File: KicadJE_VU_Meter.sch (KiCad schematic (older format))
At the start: 62 parts, among them J1 Out, J2 In1, J3 In2, P1 HEADER_2x5_Doepfer, U1 TL072, U2 TL072

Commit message: Update KicadJE_VU_Meter.sch
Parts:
- added H6: Jack, AJ:Jack_6m3, symbol Mechanical:MountingHole_Pad
- added H7, H8, H?: Jack, AJ:Jack_3m5, symbol Mechanical:MountingHole_Pad
- added J?: Out, Connector_PinHeader_2.54mm:PinHeader_1x03_P2.54mm_Vertical_SMD_Pin1Right, symbol Connector:Conn_01x03_Male
- added MES2: VU Meter Backlight, Connector_PinHeader_2.54mm:PinHeader_1x02_P2.54mm_Vertical_SMD_Pin1Right, symbol Device:Amperemeter_AC
- added R?: 1k, Resistor_SMD:R_0805_2012Metric_Pad1.20x1.40mm_HandSolder, symbol Device:R
- added R?: OPEN, Resistor_SMD:R_0805_2012Metric_Pad1.20x1.40mm_HandSolder, symbol Device:R
- added TP?: Out, TestPoint:TestPoint_Pad_D2.0mm, symbol Connector:TestPoint
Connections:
- net -12VA: now also MES2.1
- net GND: now also H6.1, H7.1, H8.1, H?.1, MES2.2
- net Out1: now also R?.1
- new net: J?.2 (Pin_2), R?.2, R?.2
- new net: J?.1 (Pin_1), R?.1, TP?.1
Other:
- moved on the sheet: H5
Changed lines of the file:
@@
 L Mechanical:MountingHole H5
 U 1 1 5EF9702E
-P 9100 4750
-F 0 "H5" H 9200 4796 50  0000 L CNN
-F 1 "Meter" H 9200 4705 50  0000 L CNN
-F 2 "AJ:VU_Meter_Hole" H 9100 4750 50  0001 C CNN
-F 3 "~" H 9100 4750 50  0001 C CNN
-	1    9100 4750
+P 8850 4675
+F 0 "H5" H 8950 4721 50  0000 L CNN
+F 1 "Meter" H 8950 4630 50  0000 L CNN
+F 2 "AJ:VU_Meter_Hole" H 8850 4675 50  0001 C CNN
+F 3 "~" H 8850 4675 50  0001 C CNN
+	1    8850 4675
 	1    0    0    -1
 $EndComp
@@
 Wire Wire Line
 	1950 7100 1950 7475
+$Comp
+L Device:Amperemeter_AC MES2
+U 1 1 60A9F992
+P 9300 5150
+F 0 "MES2" H 9453 5196 50  0000 L CNN
+F 1 "VU Meter Backlight" H 9453 5105 50  0000 L CNN
+F 2 "Connector_PinHeader_2.54mm:PinHeader_1x02_P2.54mm_Vertical_SMD_Pin1Right" V 9300 5250 50  0001 C CNN
+F 3 "~" V 9300 5250 50  0001 C CNN
+	1    9300 5150
+	1    0    0    -1
+$EndComp
+$Comp
+L KicadJE_VU_Meter-rescue:GND-Envelope-cache-2018-08-04-13-00-04-KicadJE_Util-rescue #PWR0101
+U 1 1 60AA0119
+P 9150 4825
+AR Path="/60AA0119" Ref="#PWR0101"  Part="1"
+AR Path="/5C8C5FC0/60AA0119" Ref="#PWR?"  Part="1"
+AR Path="/5CAAE8D3/60AA0119" Ref="#PWR?"  Part="1"
+AR Path="/5E4B0DD9/60AA0119" Ref="#PWR?"  Part="1"
+AR Path="/5E62ACA1/60AA0119" Ref="#PWR?"  Part="1"
+AR Path="/5F49A670/60AA0119" Ref="#PWR?"  Part="1"
+F 0 "#PWR0101" H 9150 4575 50  0001 C CNN
+F 1 "GND" H 9155 4652 50  0000 C CNN
+F 2 "" H 9150 4825 50  0001 C CNN
+F 3 "" H 9150 4825 50  0001 C CNN
+	1    9150 4825
+	1    0    0    -1
+$EndComp
+$Comp
+L power:-12VA #PWR?
+U 1 1 60AA116C
+P 9300 5425
+AR Path="/5E4B0DD9/60AA116C" Ref="#PWR?"  Part="1"
+AR Path="/5E62ACA1/60AA116C" Ref="#PWR?"  Part="1"
+AR Path="/5F49A670/60AA116C" Ref="#PWR?"  Part="1"
+AR Path="/60AA116C" Ref="#PWR0102"  Part="1"
+F 0 "#PWR0102" H 9300 5275 50  0001 C CNN
+F 1 "-12VA" H 9450 5500 50  0000 C CNN
+F 2 "" H 9300 5425 50  0001 C CNN
+F 3 "" H 9300 5425 50  0001 C CNN
+	1    9300 5425
+	-1   0    0    1
+$EndComp
+Wire Wire Line
+	9300 5425 9300 5350
+Wire Wire Line
+	9300 4950 9300 4800
+Wire Wire Line
+	9300 4800 9150 4800
+Wire Wire Line
+	9150 4800 9150 4825
+$Comp
+L Mechanical:MountingHole_Pad H7
+U 1 1 60ABB9E2
+P 1500 2700
+F 0 "H7" H 1600 2749 50  0000 L CNN
+F 1 "Jack" H 1600 2658 50  0000 L CNN
+F 2 "AJ:Jack_3m5" H 1500 2700 50  0001 C CNN
+F 3 "~" H 1500 2700 50  0001 C CNN
+	1    1500 2700
+	1    0    0    -1
+$EndComp
+$Comp
+L Mechanical:MountingHole_Pad H8
+U 1 1 60ABC029
+P 1500 4075
+F 0 "H8" H 1600 4124 50  0000 L CNN
+F 1 "Jack" H 1600 4033 50  0000 L CNN
+F 2 "AJ:Jack_3m5" H 1500 4075 50  0001 C CNN
+F 3 "~" H 1500 4075 50  0001 C CNN
+	1    1500 4075
+	1    0    0    -1
+$EndComp
+$Comp
+L KicadJE_VU_Meter-rescue:GND-Envelope-cache-2018-08-04-13-00-04-KicadJE_Util-rescue #PWR0103
+U 1 1 60ABC354
+P 1500 4175
+AR Path="/60ABC354" Ref="#PWR0103"  Part="1"
+AR Path="/5C8C5FC0/60ABC354" Ref="#PWR?"  Part="1"
+AR Path="/5CAAE8D3/60ABC354" Ref="#PWR?"  Part="1"
+AR Path="/5E4B0DD9/60ABC354" Ref="#PWR?"  Part="1"
+AR Path="/5E62ACA1/60ABC354" Ref="#PWR?"  Part="1"
+AR Path="/5F49A670/60ABC354" Ref="#PWR?"  Part="1"
+F 0 "#PWR0103" H 1500 3925 50  0001 C CNN
+F 1 "GND" H 1505 4002 50  0000 C CNN
+F 2 "" H 1500 4175 50  0001 C CNN
+F 3 "" H 1500 4175 50  0001 C CNN
+	1    1500 4175
+	1    0    0    -1
+$EndComp
+$Comp
+L KicadJE_VU_Meter-rescue:GND-Envelope-cache-2018-08-04-13-00-04-KicadJE_Util-rescue #PWR0104
+U 1 1 60ABC5DE
+P 1500 2800
+AR Path="/60ABC5DE" Ref="#PWR0104"  Part="1"
+AR Path="/5C8C5FC0/60ABC5DE" Ref="#PWR?"  Part="1"
+AR Path="/5CAAE8D3/60ABC5DE" Ref="#PWR?"  Part="1"
+AR Path="/5E4B0DD9/60ABC5DE" Ref="#PWR?"  Part="1"
+AR Path="/5E62ACA1/60ABC5DE" Ref="#PWR?"  Part="1"
+AR Path="/5F49A670/60ABC5DE" Ref="#PWR?"  Part="1"
+F 0 "#PWR0104" H 1500 2550 50  0001 C CNN
+F 1 "GND" H 1505 2627 50  0000 C CNN
+F 2 "" H 1500 2800 50  0001 C CNN
+F 3 "" H 1500 2800 50  0001 C CNN
+	1    1500 2800
+	1    0    0    -1
+$EndComp
+$Comp
+L Mechanical:MountingHole_Pad H6
+U 1 1 60ACF365
+P 925 5375
+F 0 "H6" H 1025 5424 50  0000 L CNN
+F 1 "Jack" H 1025 5333 50  0000 L CNN
+F 2 "AJ:Jack_6m3" H 925 5375 50  0001 C CNN
+F 3 "~" H 925 5375 50  0001 C CNN
+	1    925  5375
+	1    0    0    -1
+$EndComp
+$Comp
+L KicadJE_VU_Meter-rescue:GND-Envelope-cache-2018-08-04-13-00-04-KicadJE_Util-rescue #PWR0105
+U 1 1 60ACFCBF
+P 925 5475
+AR Path="/60ACFCBF" Ref="#PWR0105"  Part="1"
+AR Path="/5C8C5FC0/60ACFCBF" Ref="#PWR?"  Part="1"
+AR Path="/5CAAE8D3/60ACFCBF" Ref="#PWR?"  Part="1"
+AR Path="/5E4B0DD9/60ACFCBF" Ref="#PWR?"  Part="1"
+AR Path="/5E62ACA1/60ACFCBF" Ref="#PWR?"  Part="1"
+AR Path="/5F49A670/60ACFCBF" Ref="#PWR?"  Part="1"
+F 0 "#PWR0105" H 925 5225 50  0001 C CNN
+F 1 "GND" H 930 5302 50  0000 C CNN
+F 2 "" H 925 5475 50  0001 C CNN
+F 3 "" H 925 5475 50  0001 C CNN
+	1    925  5475
+	1    0    0    -1
+$EndComp
+$Comp
+L Mechanical:MountingHole_Pad H?
+U 1 1 60AF0323
+P 700 5375
+F 0 "H?" H 800 5424 50  0000 L CNN
+F 1 "Jack" H 800 5333 50  0000 L CNN
+F 2 "AJ:Jack_3m5" H 700 5375 50  0001 C CNN
+F 3 "~" H 700 5375 50  0001 C CNN
+	1    700  5375
+	1    0    0    -1
+$EndComp
+Wire Wire Line
+	700  5475 925  5475
+Connection ~ 925  5475
+Wire Wire Line
+	1550 5725 1475 5725
+Wire Wire Line
+	2375 5825 2425 5825
+$Comp
+L Device:R R?
+U 1 1 60AFA9E5
+P 2225 5825
+AR Path="/60AFA9E5" Ref="R?"  Part="1"
+AR Path="/5C8C5FC0/60AFA9E5" Ref="R?"  Part="1"
+AR Path="/5CAAE8D3/60AFA9E5" Ref="R?"  Part="1"
+AR Path="/5E4B0DD9/60AFA9E5" Ref="R?"  Part="1"
+AR Path="/5F49A670/60AFA9E5" Ref="R?"  Part="1"
+F 0 "R?" V 2100 5825 50  0000 C CNN
+F 1 "1k" V 2225 5825 50  0000 C CNN
+F 2 "Resistor_SMD:R_0805_2012Metric_Pad1.20x1.40mm_HandSolder" V 2155 5825 50  0001 C CNN
+F 3 "~" H 2225 5825 50  0001 C CNN
+	1    2225 5825
+	0    1    1    0
+$EndComp
+Wire Wire Line
+	1550 5725 1550 6000
+$Comp
+L Connector:TestPoint TP?
+U 1 1 60AFA9F0
+P 1475 5725
+F 0 "TP?" H 1533 5843 50  0000 L CNN
+F 1 "Out" H 1533 5752 50  0000 L CNN
+F 2 "TestPoint:TestPoint_Pad_D2.0mm" H 1675 5725 50  0001 C CNN
+F 3 "~" H 1675 5725 50  0001 C CNN
+	1    1475 5725
+	1    0    0    -1
+$EndComp
+Connection ~ 1475 5725
+Wire Wire Line
+	1475 5725 1400 5725
+$Comp
+L Device:R R?
+U 1 1 60AFA9FC
+P 1800 6000
+AR Path="/60AFA9FC" Ref="R?"  Part="1"
+AR Path="/5C8C5FC0/60AFA9FC" Ref="R?"  Part="1"
+AR Path="/5CAAE8D3/60AFA9FC" Ref="R?"  Part="1"
+AR Path="/5E4B0DD9/60AFA9FC" Ref="R?"  Part="1"
+AR Path="/5E62ACA1/60AFA9FC" Ref="R?"  Part="1"
+AR Path="/5F49A670/60AFA9FC" Ref="R?"  Part="1"
+F 0 "R?" V 1875 6075 50  0000 C CNN
+F 1 "OPEN" V 1800 6000 50  0000 C CNN
+F 2 "Resistor_SMD:R_0805_2012Metric_Pad1.20x1.40mm_HandSolder" V 1730 6000 50  0001 C CNN
+F 3 "~" H 1800 6000 50  0001 C CNN
+	1    1800 6000
+	0    -1   -1   0
+$EndComp
+Wire Wire Line
+	1650 6000 1550 6000
+Wire Wire Line
+	1950 6000 2000 6000
+Wire Wire Line
+	2000 6000 2000 5825
+Wire Wire Line
+	1400 5825 2000 5825
+Connection ~ 2000 5825
+Wire Wire Line
+	2000 5825 2075 5825
+$Comp
+L Connector:Conn_01x03_Male J?
+U 1 1 60AFAA0C
+P 1200 5825
+F 0 "J?" H 1308 6106 50  0000 C CNN
+F 1 "Out" H 1308 6015 50  0000 C CNN
+F 2 "Connector_PinHeader_2.54mm:PinHeader_1x03_P2.54mm_Vertical_SMD_Pin1Right" H 1200 5825 50  0001 C CNN
+F 3 "~" H 1200 5825 50  0001 C CNN
+	1    1200 5825
+	1    0    0    -1
+$EndComp
+Wire Wire Line
+	2425 5825 2425 5325
 $EndSCHEMATC

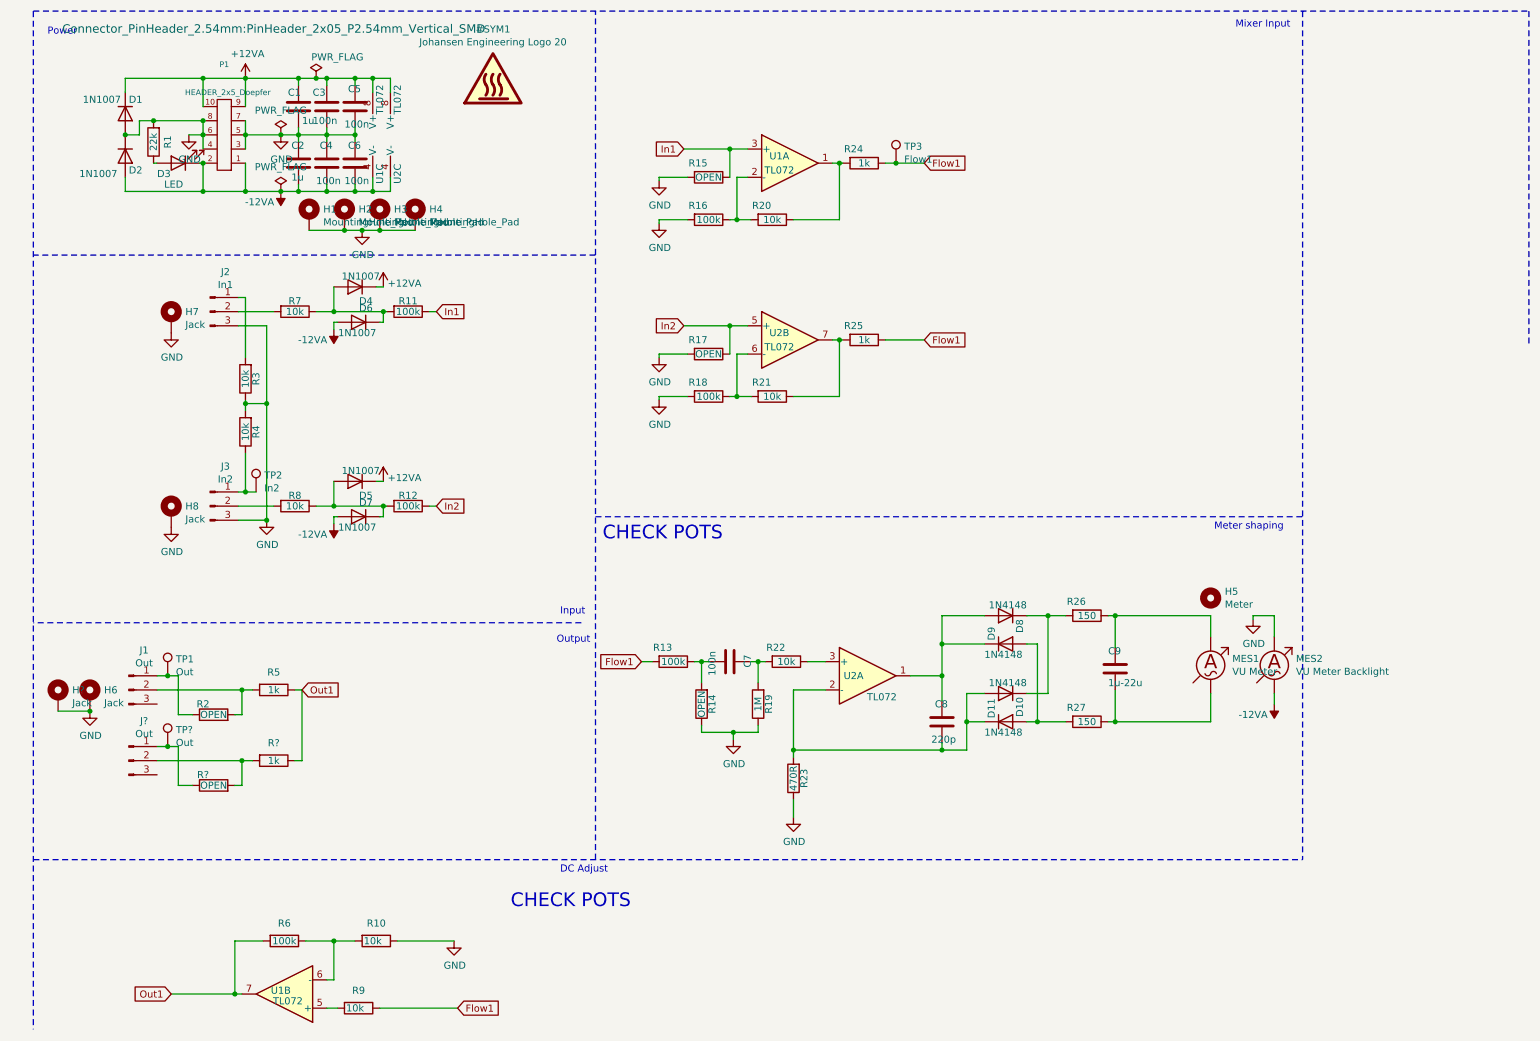
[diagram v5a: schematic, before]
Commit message: Removed second op amp
save space
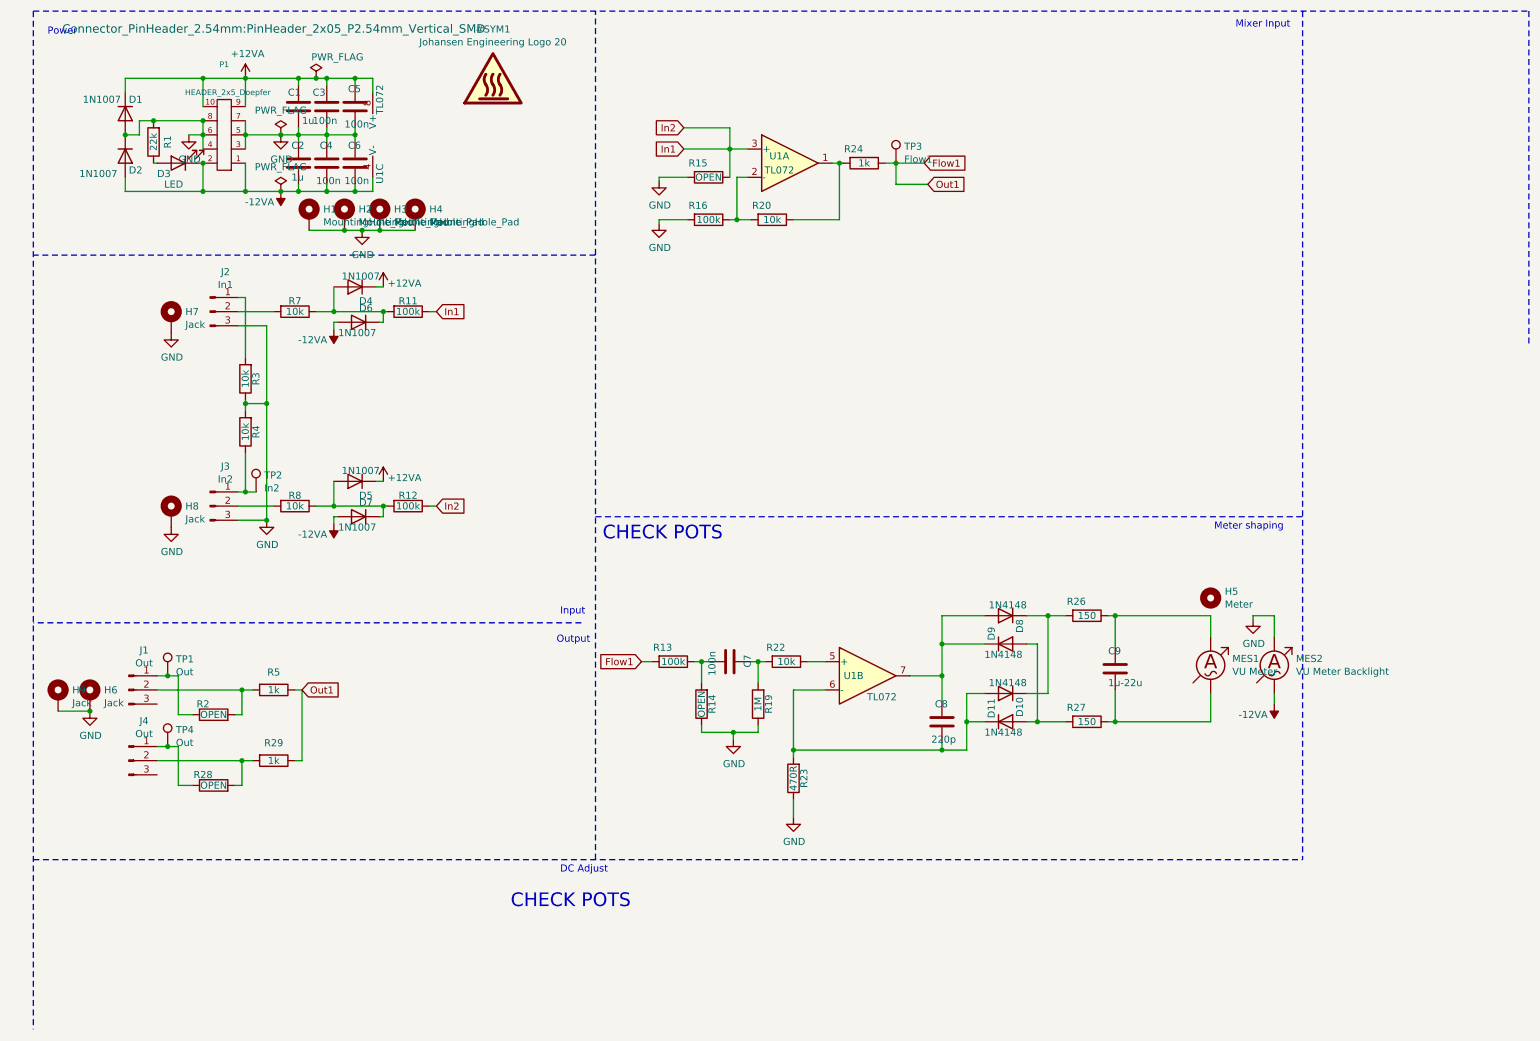
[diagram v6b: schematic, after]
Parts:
- removed R10, R21, R9: 10k, Resistor_SMD:R_0805_2012Metric_Pad1.20x1.40mm_HandSolder, symbol Device:R
- removed R17: OPEN, Resistor_SMD:R_0805_2012Metric_Pad1.20x1.40mm_HandSolder, symbol Device:R
- removed R18, R6: 100k, Resistor_SMD:R_0805_2012Metric_Pad1.20x1.40mm_HandSolder, symbol Device:R
- removed R25: 1k, Resistor_SMD:R_0805_2012Metric_Pad1.20x1.40mm_HandSolder, symbol Device:R
- removed unit 2 of U1
- removed unit 3 of U2
- removed unit 2 of U2
- gave numbers to parts that had none: 5
- renumbered U2 to U1
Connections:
- net In2 is gone; now on net In1: R12.1
- net Out1 is gone; now on net Flow1: R29.1, R5.1
- net at C8.1, D8.2 (A), D9.1 (K): now also U1.7; no longer U1.1
- net at C8.2, D10.2 (A), D11.1 (K)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: now also U1.6 (-); no longer U1.2 (-)
- net at R22.1: now also U1.5 (+); no longer U1.3 (+)
